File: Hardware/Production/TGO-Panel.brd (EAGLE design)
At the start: 25.4 x 25.4 mm, 59 parts, among them U1 AP3012, U2 SAS1-1U001-A_I2C_4WSPI

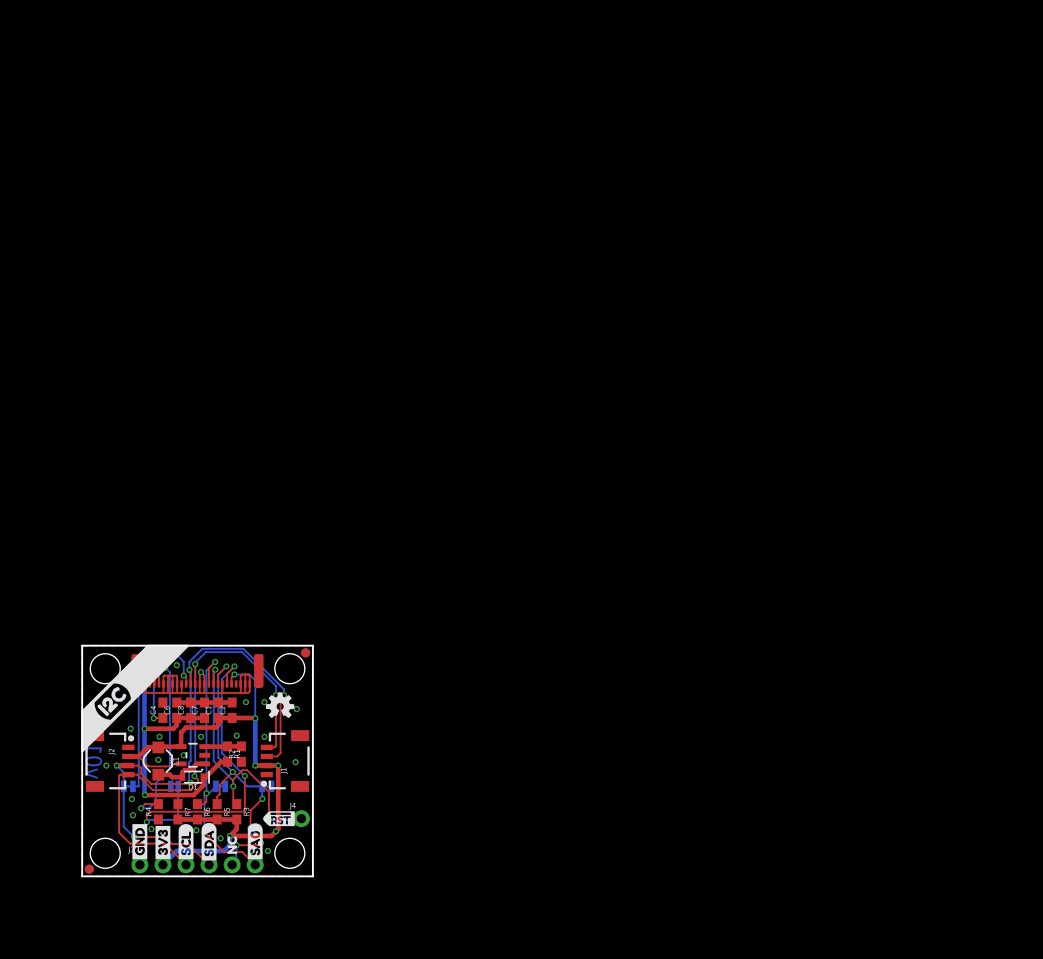
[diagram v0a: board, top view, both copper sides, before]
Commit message: Proto review changes
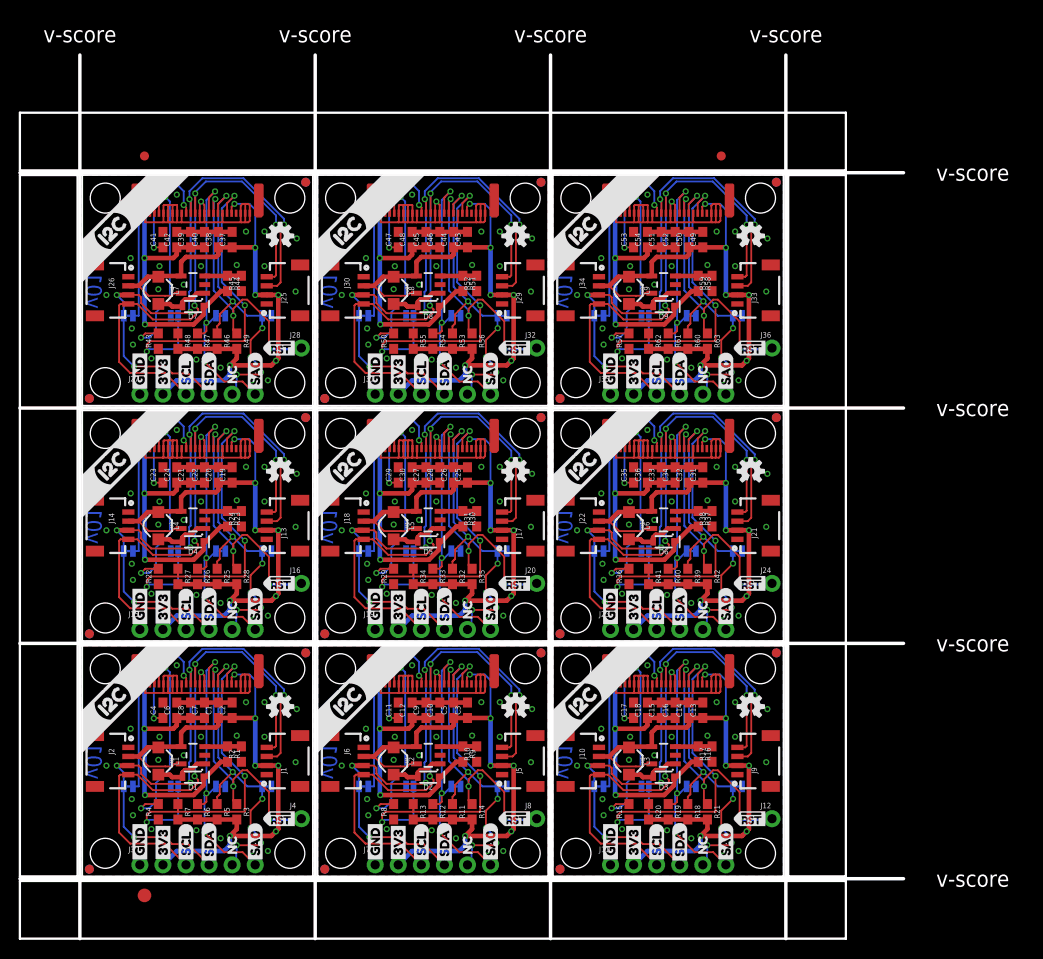
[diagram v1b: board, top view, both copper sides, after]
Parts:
- removed FRAME1: FRAME-LETTER, SparkFun-Aesthetics:CREATIVE_COMMONS
- added C10, C11, C12, C14, C16, C17, C18, C20, C22, C23, C24, C26, C28, C29, C30, C32, C34, C35, C36, C38, C40, C41, C42, C44, C46, C47, C48, C5, C50, C52, C53, C54: 4.7uF, SparkFun-Capacitors:0603
- added C13, C15, C19, C21, C25, C27, C3, C31, C33, C37, C39, C43, C45, C49, C51, C9: 0.1uF, SparkFun-Capacitors:0603
- added D2, D3, D4, D5, D6, D7, D8, D9: 1A/23V/620mV, SparkFun-DiscreteSemi:SOD-323
- added E$1, E$2: (no value), SparkFun-Aesthetics:FIDUCIAL-1X2
- added E$3: (no value), SparkFun-Retired:FIDUCIAL-1.5X3
- added FD10, FD11, FD12, FD13, FD14, FD15, FD16, FD17, FD18, FD19, FD20, FD21, FD22, FD23, FD24, FD25, FD26, FD27, FD28, FD29, FD30, FD31, FD32, FD33, FD34, FD35, FD36, FD5, FD6, FD7, FD8, FD9: FIDUCIAL1X2, SparkFun-Aesthetics:FIDUCIAL-1X2
- added J10, J13, J14, J17, J18, J21, J22, J25, J26, J29, J30, J33, J34, J5, J6, J9: (no value), SparkFun-Connectors:1X04_1MM_RA
- added J11, J15, J19, J23, J27, J31, J35, J7: (no value), SparkFun-Connectors:1X06_NO_SILK
- added J12, J16, J20, J24, J28, J32, J36, J8: (no value), SparkFun-Connectors:1X01_NO_SILK
- added JP10, JP14, JP18, JP22, JP26, JP30, JP34, JP6: SAS, SparkFun-Jumpers:SMT-JUMPER_2_NC_TRACE_SILK
- added JP11, JP15, JP19, JP23, JP27, JP31, JP35, JP7: IFS, SparkFun-Jumpers:SMT-JUMPER_2_NO_SILK
- added JP12, JP16, JP20, JP24, JP28, JP32, JP36, JP8: I2C, SparkFun-Jumpers:SMT-JUMPER_2_NC_TRACE_SILK
- added JP13, JP17, JP21, JP25, JP29, JP33, JP5, JP9: CSP, SparkFun-Jumpers:SMT-JUMPER_2_NC_TRACE_SILK
- added L2, L3, L4, L5, L6, L7, L8, L9: 10uH, SparkFun-Coils:INDUCTOR_4.7UH
- added LOGO10, LOGO12, LOGO14, LOGO16, LOGO18, LOGO4, LOGO6, LOGO8: SFE_LOGO_NAME_FLAME.1_INCH, SparkFun-Aesthetics:SFE_LOGO_NAME_FLAME_.1
- added LOGO11, LOGO13, LOGO15, LOGO17, LOGO3, LOGO5, LOGO7, LOGO9: OSHW-LOGOS, SparkFun-Aesthetics:OSHW-LOGO-S
- added R10, R17, R24, R31, R38, R45, R52, R59: 5.6k, SparkFun-Resistors:0603
- added R11, R12, R13, R14, R18, R19, R20, R21, R25, R26, R27, R28, R32, R33, R34, R35, R39, R40, R41, R42, R46, R47, R48, R49, R53, R54, R55, R56, R60, R61, R62, R63: 10k, SparkFun-Resistors:0603
- added R15, R22, R29, R36, R43, R50, R57, R8: 100k, SparkFun-Resistors:0603
- added R16, R23, R30, R37, R44, R51, R58, R9: 47k, SparkFun-Resistors:0603
- added U$100, U$127, U$154, U$181, U$208, U$235, U$46, U$73: (no value), buzzard_labels_1:#RST0
- added U$101, U$128, U$155, U$182, U$209, U$236, U$47, U$74: (no value), buzzard_labels_1:#RST1
- added U$102, U$129, U$156, U$183, U$210, U$237, U$48, U$75: (no value), buzzard_labels_1:I2C3
- added U$103, U$130, U$157, U$184, U$211, U$238, U$49, U$76: (no value), buzzard_labels_1:SPI2
- added U$104, U$131, U$158, U$185, U$212, U$239, U$50, U$77: (no value), buzzard_labels_1:SA05
- added U$105, U$132, U$159, U$186, U$213, U$240, U$51, U$78: (no value), buzzard_labels_1:#CS4
- added U$106, U$133, U$160, U$187, U$214, U$241, U$52, U$79: (no value), buzzard_labels_1:SPI6
- added U$107, U$108, U$134, U$135, U$161, U$162, U$188, U$189, U$215, U$216, U$242, U$243, U$53, U$54, U$80, U$81: (no value), buzzard_labels_1:D27
- added U$109, U$136, U$163, U$190, U$217, U$25, U$55, U$82: QWIIC_BOARD_OUTLINEH, SparkX:QWIIC_BOARD_MOUNT_HOLES
- added U$110, U$120, U$137, U$147, U$164, U$174, U$191, U$201, U$218, U$228, U$27, U$39, U$56, U$66, U$83, U$93: (no value), buzzard_labels:GND0
- added U$111, U$119, U$138, U$146, U$165, U$173, U$192, U$200, U$219, U$227, U$30, U$38, U$57, U$65, U$84, U$92: (no value), buzzard_labels:3V31
- added U$112, U$139, U$166, U$193, U$220, U$31, U$58, U$85: (no value), buzzard_labels:SCL2
- added U$113, U$140, U$167, U$194, U$221, U$32, U$59, U$86: (no value), buzzard_labels:SDA3
- added U$114, U$141, U$168, U$195, U$222, U$33, U$60, U$87: (no value), buzzard_labels:SA08
- added U$115, U$142, U$169, U$196, U$223, U$34, U$61, U$88: (no value), buzzard_labels:NC10
- added U$116, U$143, U$170, U$197, U$224, U$35, U$62, U$89: (no value), buzzard_labels:#CS7
- added U$117, U$144, U$171, U$198, U$225, U$36, U$63, U$90: (no value), buzzard_labels:MOSI9
- added U$118, U$145, U$172, U$199, U$226, U$37, U$64, U$91: (no value), buzzard_labels:SCLK8
- added U$121, U$148, U$175, U$202, U$229, U$40, U$67, U$94: (no value), buzzard_labels:D##C6
- added U$122, U$149, U$176, U$203, U$230, U$41, U$68, U$95: (no value), buzzard_labels:GND10
- added U$123, U$150, U$177, U$204, U$231, U$42, U$69, U$96: (no value), buzzard_labels:013
- added U$124, U$151, U$178, U$205, U$232, U$43, U$70, U$97: (no value), buzzard_labels:I2C13
- added U$125, U$152, U$179, U$206, U$233, U$44, U$71, U$98: (no value), buzzard_labels:QWIIC_TRANSPARENT_GRAPHICAL_OLED15
- added U$126, U$153, U$180, U$207, U$234, U$45, U$72, U$99: (no value), buzzard_labels:IFS17
- added U10, U12, U14, U16, U18, U4, U6, U8: AP3012, SparkFun-IC-Power:SOT23-5
- added U11, U13, U15, U17, U3, U5, U7, U9: SAS1-1U001-A_I2C_4WSPI, TGO:FPC05024-42201
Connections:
- new net !CS1: J7.5, JP5.2, R11.1, U3.P$8
- new net !CS2: J11.5, JP9.2, R18.1, U5.P$8
- new net !CS3: J15.5, JP13.2, R25.1, U7.P$8
- new net !CS4: J19.5, JP17.2, R32.1, U9.P$8
- new net !CS5: J23.5, JP21.2, R39.1, U11.P$8
- new net !CS6: J27.5, JP25.2, R46.1, U13.P$8
- new net !CS7: J31.5, JP29.2, R53.1, U15.P$8
- new net !CS8: J35.5, JP33.2, R60.1, U17.P$8
- new net !RES1: J8.1, R14.1, U3.P$9
- new net !RES2: J12.1, R21.1, U5.P$9
- new net !RES3: J16.1, R28.1, U7.P$9
- new net !RES4: J20.1, R35.1, U9.P$9
- new net !RES5: J24.1, R42.1, U11.P$9
- new net !RES6: J28.1, R49.1, U13.P$9
- new net !RES7: J32.1, R56.1, U15.P$9
- new net !RES8: J36.1, R63.1, U17.P$9
- new net 12V1: C10.1, C12.1, C9.1, D2.C, R9.2, U3.P$23
- new net 12V2: C15.1, C16.1, C18.1, D3.C, R16.2, U5.P$23
- new net 12V3: C21.1, C22.1, C24.1, D4.C, R23.2, U7.P$23
- new net 12V4: C27.1, C28.1, C30.1, D5.C, R30.2, U9.P$23
- new net 12V5: C33.1, C34.1, C36.1, D6.C, R37.2, U11.P$23
- new net 12V6: C39.1, C40.1, C42.1, D7.C, R44.2, U13.P$23
- new net 12V7: C45.1, C46.1, C48.1, D8.C, R51.2, U15.P$23
- new net 12V8: C51.1, C52.1, C54.1, D9.C, R58.2, U17.P$23
- new net 3.3V1: C3.1, C5.1, J5.2, J6.2, J7.2, L2.P$1, R11.2, R12.2, R13.2, R14.2, U3.P$5, U4.4, U4.5
- new net 3.3V2: C13.1, C14.1, J10.2, J11.2, J9.2, L3.P$1, R18.2, R19.2, R20.2, R21.2, U5.P$5, U6.4, U6.5
- new net 3.3V3: C19.1, C20.1, J13.2, J14.2, J15.2, L4.P$1, R25.2, R26.2, R27.2, R28.2, U7.P$5, U8.4, U8.5
- new net 3.3V4: C25.1, C26.1, J17.2, J18.2, J19.2, L5.P$1, R32.2, R33.2, R34.2, R35.2, U10.4, U10.5, U9.P$5
- new net 3.3V5: C31.1, C32.1, J21.2, J22.2, J23.2, L6.P$1, R39.2, R40.2, R41.2, R42.2, U11.P$5, U12.4, U12.5
- new net 3.3V6: C37.1, C38.1, J25.2, J26.2, J27.2, L7.P$1, R46.2, R47.2, R48.2, R49.2, U13.P$5, U14.4, U14.5
- new net 3.3V7: C43.1, C44.1, J29.2, J30.2, J31.2, L8.P$1, R53.2, R54.2, R55.2, R56.2, U15.P$5, U16.4, U16.5
- new net 3.3V8: C49.1, C50.1, J33.2, J34.2, J35.2, L9.P$1, R60.2, R61.2, R62.2, R63.2, U17.P$5, U18.4, U18.5
- new net D!C!/SA1: J7.6, JP6.2, R12.1, U3.P$10
- new net D!C!/SA2: J11.6, JP10.2, R19.1, U5.P$10
- new net D!C!/SA3: J15.6, JP14.2, R26.1, U7.P$10
- new net D!C!/SA4: J19.6, JP18.2, R33.1, U9.P$10
- new net D!C!/SA5: J23.6, JP22.2, R40.1, U11.P$10
- new net D!C!/SA6: J27.6, JP26.2, R47.1, U13.P$10
- new net D!C!/SA7: J31.6, JP30.2, R54.1, U15.P$10
- new net D!C!/SA8: J35.6, JP34.2, R61.1, U17.P$10
- new net GND1: C10.2, C11.2, C12.2, C3.2, C5.2, C9.2, J5.1, J6.1, J7.1, JP5.1, JP6.1, JP7.2, R10.1, R8.1, U3.P$1, U3.P$11, U3.P$12, U3.P$16, U3.P$17, U3.P$18, U3.P$19, U3.P$2, U3.P$20, U3.P$24, U3.P$3, U3.P$7, U4.2
- new net GND2: C13.2, C14.2, C15.2, C16.2, C17.2, C18.2, J10.1, J11.1, J9.1, JP10.1, JP11.2, JP9.1, R15.1, R17.1, U5.P$1, U5.P$11, U5.P$12, U5.P$16, U5.P$17, U5.P$18, U5.P$19, U5.P$2, U5.P$20, U5.P$24, U5.P$3, U5.P$7, U6.2
- new net GND3: C19.2, C20.2, C21.2, C22.2, C23.2, C24.2, J13.1, J14.1, J15.1, JP13.1, JP14.1, JP15.2, R22.1, R24.1, U7.P$1, U7.P$11, U7.P$12, U7.P$16, U7.P$17, U7.P$18, U7.P$19, U7.P$2, U7.P$20, U7.P$24, U7.P$3, U7.P$7, U8.2
- new net GND4: C25.2, C26.2, C27.2, C28.2, C29.2, C30.2, J17.1, J18.1, J19.1, JP17.1, JP18.1, JP19.2, R29.1, R31.1, U10.2, U9.P$1, U9.P$11, U9.P$12, U9.P$16, U9.P$17, U9.P$18, U9.P$19, U9.P$2, U9.P$20, U9.P$24, U9.P$3, U9.P$7
- new net GND5: C31.2, C32.2, C33.2, C34.2, C35.2, C36.2, J21.1, J22.1, J23.1, JP21.1, JP22.1, JP23.2, R36.1, R38.1, U11.P$1, U11.P$11, U11.P$12, U11.P$16, U11.P$17, U11.P$18, U11.P$19, U11.P$2, U11.P$20, U11.P$24, U11.P$3, U11.P$7, U12.2
- new net GND6: C37.2, C38.2, C39.2, C40.2, C41.2, C42.2, J25.1, J26.1, J27.1, JP25.1, JP26.1, JP27.2, R43.1, R45.1, U13.P$1, U13.P$11, U13.P$12, U13.P$16, U13.P$17, U13.P$18, U13.P$19, U13.P$2, U13.P$20, U13.P$24, U13.P$3, U13.P$7, U14.2
- new net GND7: C43.2, C44.2, C45.2, C46.2, C47.2, C48.2, J29.1, J30.1, J31.1, JP29.1, JP30.1, JP31.2, R50.1, R52.1, U15.P$1, U15.P$11, U15.P$12, U15.P$16, U15.P$17, U15.P$18, U15.P$19, U15.P$2, U15.P$20, U15.P$24, U15.P$3, U15.P$7, U16.2
- new net GND8: C49.2, C50.2, C51.2, C52.2, C53.2, C54.2, J33.1, J34.1, J35.1, JP33.1, JP34.1, JP35.2, R57.1, R59.1, U17.P$1, U17.P$11, U17.P$12, U17.P$16, U17.P$17, U17.P$18, U17.P$19, U17.P$2, U17.P$20, U17.P$24, U17.P$3, U17.P$7, U18.2
- new net I2C!4WSPI1: JP7.1, R13.1, U3.P$6
- new net I2C!4WSPI2: JP11.1, R20.1, U5.P$6
- new net I2C!4WSPI3: JP15.1, R27.1, U7.P$6
- new net I2C!4WSPI4: JP19.1, R34.1, U9.P$6
- new net I2C!4WSPI5: JP23.1, R41.1, U11.P$6
- new net I2C!4WSPI6: JP27.1, R48.1, U13.P$6
- new net I2C!4WSPI7: JP31.1, R55.1, U15.P$6
- new net I2C!4WSPI8: JP35.1, R62.1, U17.P$6
- new net N$10: R15.2, U5.P$21
- new net N$11: D3.A, L3.P$2, U6.1
- new net N$12: R16.1, R17.2, U6.3
- new net N$13: C23.1, U7.P$22
- new net N$14: R22.2, U7.P$21
- new net N$15: D4.A, L4.P$2, U8.1
- new net N$16: R23.1, R24.2, U8.3
- new net N$17: C29.1, U9.P$22
- new net N$18: R29.2, U9.P$21
- new net N$19: D5.A, L5.P$2, U10.1
- new net N$2: C11.1, U3.P$22
- new net N$20: R30.1, R31.2, U10.3
- new net N$21: C35.1, U11.P$22
- new net N$22: R36.2, U11.P$21
- new net N$23: D6.A, L6.P$2, U12.1
- new net N$24: R37.1, R38.2, U12.3
- new net N$25: C41.1, U13.P$22
- new net N$26: R43.2, U13.P$21
- new net N$27: D7.A, L7.P$2, U14.1
- new net N$28: R44.1, R45.2, U14.3
- new net N$29: C47.1, U15.P$22
- new net N$30: R50.2, U15.P$21
- new net N$31: D8.A, L8.P$2, U16.1
- new net N$32: R51.1, R52.2, U16.3
- new net N$33: C53.1, U17.P$22
- new net N$34: R57.2, U17.P$21
- new net N$35: D9.A, L9.P$2, U18.1
- new net N$36: R58.1, R59.2, U18.3
- new net N$6: R8.2, U3.P$21
- new net N$7: D2.A, L2.P$2, U4.1
- new net N$8: R10.2, R9.1, U4.3
- new net N$9: C17.1, U5.P$22
- new net NC/D1: JP8.1, U3.P$15
- new net NC/D3: JP12.1, U5.P$15
- new net NC/D4: JP16.1, U7.P$15
- new net NC/D5: JP20.1, U9.P$15
- new net NC/D6: JP24.1, U11.P$15
- new net NC/D7: JP28.1, U13.P$15
- new net NC/D8: JP32.1, U15.P$15
- new net NC/D9: JP36.1, U17.P$15
- new net SCLK/SCL1: J5.4, J6.4, J7.3, U3.P$13
- new net SCLK/SCL2: J10.4, J11.3, J9.4, U5.P$13
- new net SCLK/SCL3: J13.4, J14.4, J15.3, U7.P$13
- new net SCLK/SCL4: J17.4, J18.4, J19.3, U9.P$13
- new net SCLK/SCL5: J21.4, J22.4, J23.3, U11.P$13
- new net SCLK/SCL6: J25.4, J26.4, J27.3, U13.P$13
- new net SCLK/SCL7: J29.4, J30.4, J31.3, U15.P$13
- new net SCLK/SCL8: J33.4, J34.4, J35.3, U17.P$13
- new net SDIN/SDA1: J5.3, J6.3, J7.4, JP8.2, U3.P$14
- new net SDIN/SDA2: J10.3, J11.4, J9.3, JP12.2, U5.P$14
- new net SDIN/SDA3: J13.3, J14.3, J15.4, JP16.2, U7.P$14
- new net SDIN/SDA4: J17.3, J18.3, J19.4, JP20.2, U9.P$14
- new net SDIN/SDA5: J21.3, J22.3, J23.4, JP24.2, U11.P$14
- new net SDIN/SDA6: J25.3, J26.3, J27.4, JP28.2, U13.P$14
- new net SDIN/SDA7: J29.3, J30.3, J31.4, JP32.2, U15.P$14
- new net SDIN/SDA8: J33.3, J34.3, J35.4, JP36.2, U17.P$14
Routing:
- net 3.3V8: track 0.00 -> 68.6 mm, vias 0 -> 6
- net 3.3V7: track 0.00 -> 68.6 mm, vias 0 -> 6
- net 3.3V6: track 0.00 -> 68.6 mm, vias 0 -> 6
- net 3.3V5: track 0.00 -> 68.6 mm, vias 0 -> 6
- net 3.3V3: track 0.00 -> 68.6 mm, vias 0 -> 6
- net 3.3V2: track 0.00 -> 68.6 mm, vias 0 -> 6
- net 3.3V4: track 0.00 -> 68.6 mm, vias 0 -> 6
- net 3.3V1: track 0.00 -> 68.6 mm, vias 0 -> 6
- net SDIN/SDA7: track 0.00 -> 64.3 mm, vias 0 -> 5
- net SDIN/SDA6: track 0.00 -> 64.3 mm, vias 0 -> 5
- net SDIN/SDA4: track 0.00 -> 64.3 mm, vias 0 -> 5
- net SDIN/SDA3: track 0.00 -> 64.3 mm, vias 0 -> 5
- net SDIN/SDA1: track 0.00 -> 64.3 mm, vias 0 -> 5
- net SDIN/SDA8: track 0.00 -> 64.3 mm, vias 0 -> 5
- net SDIN/SDA5: track 0.00 -> 64.3 mm, vias 0 -> 5
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- added copper zone on layer 1, net GND1
- added copper zone on layer 16, net GND1
- added copper zone on layer 1, net GND2
- added copper zone on layer 16, net GND2
- added copper zone on layer 1, net GND3
- added copper zone on layer 16, net GND3
- added copper zone on layer 1, net GND4
- added copper zone on layer 16, net GND4
- added copper zone on layer 1, net GND5
- added copper zone on layer 16, net GND5
- added copper zone on layer 1, net GND6
- added copper zone on layer 16, net GND6
- added copper zone on layer 1, net GND7
- added copper zone on layer 16, net GND7
- added copper zone on layer 1, net GND8
- added copper zone on layer 16, net GND8
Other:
- board size 25.4 x 25.4 mm -> 97.3 x 97.3 mm
- board text added: "v-score"
- board text removed: "Owen Lyke"
